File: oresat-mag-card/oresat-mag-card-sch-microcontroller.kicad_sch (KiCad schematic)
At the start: 31 parts, among them U7 MCXN947VKLT, U8 TCAN330, Y1 24 MHz

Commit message: Final mag card
Lots of polishing around best practices layout. Put in giant hole to thread the MTs from below if required for the 3U CubeSats. Cleaned up power layer, added stitching vias, updated readme.
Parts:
- C13, C14, C15, C16, C17, C18, C19, C20, C21, C22, C23, C24, C25, C26, C27, C28, C29, C30, C70, D4, R47, R76, U8, Y1: DIST DigiKey -> (none)
- FB1, L2: DIS DIgiKey -> DigiKey
- R45: DIS Digi-Key -> DigiKey
- R46, R48, U7: DIS (none) -> DigiKey; DIST DigiKey -> (none)
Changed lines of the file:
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@@
 	(title_block
 		(title "OreSat Mag Card")
-		(date "2026-04-02")
+		(date "2026-04-07")
 		(rev "v1.0")
 		(company "Portland State Aerospace Society")
@@
 			)
 		)
-		(property "DIST" "DigiKey"
+		(property "DIST" ""
 			(at 148.59 190.5 0)
 			(effects
@@
 			)
 		)
-		(property "DIST" "DigiKey"
+		(property "DIST" ""
 			(at 345.44 252.73 0)
 			(effects
@@
 			)
 		)
-		(property "DIST" "DigiKey"
+		(property "DIST" ""
 			(at 397.51 96.52 0)
 			(effects
@@
 			)
 		)
-		(property "DIST" "DigiKey"
+		(property "DIST" ""
 			(at 353.06 252.73 0)
 			(effects
@@
 			)
 		)
-		(property "DIS" "Digi-Key"
+		(property "DIS" "DigiKey"
 			(at 116.84 198.12 0)
 			(effects
@@
 			)
 		)
-		(property "DIST" "DigiKey"
+		(property "DIST" ""
 			(at 101.6 210.82 0)
 			(effects
@@
 			)
 		)
-		(property "DIST" "DigiKey"
+		(property "DPN" "568-MCXN947VDFT-ND"
 			(at 236.22 184.15 0)
 			(effects
@@
 			)
 		)
-		(property "DPN" "568-MCXN947VDFT-ND"
+		(property "DIS" "DigiKey"
+			(at 236.22 184.15 0)
+			(effects
+				(font
+					(size 1.27 1.27)
+				)
+				(hide yes)
+			)
+		)
+		(property "DIST" ""
 			(at 236.22 184.15 0)
 			(effects
@@
 			)
 		)
-		(property "DIS" "DIgiKey"
+		(property "DIS" "DigiKey"
 			(at 375.92 110.49 90)
 			(effects
@@
 			)
 		)
-		(property "DIST" "DigiKey"
+		(property "DIST" ""
 			(at 377.19 252.73 0)
 			(effects
@@
 			)
 		)
-		(property "DIST" "DigiKey"
+		(property "DIST" ""
 			(at 322.58 252.73 0)
 			(effects
@@
 			)
 		)
-		(property "DIST" "DigiKey"
+		(property "DIST" ""
 			(at 330.2 252.73 0)
 			(effects
@@
 			)
 		)
-		(property "DIST" "DigiKey"
+		(property "DIST" ""
 			(at 368.3 252.73 0)
 			(effects
@@
 			)
 		)
-		(property "DIST" "DigiKey"
+		(property "DPN" "RMCF0603FT4K70CT-ND"
 			(at 285.75 190.5 0)
 			(effects
@@
 			)
 		)
-		(property "DPN" "RMCF0603FT4K70CT-ND"
+		(property "MFR" "Stackpole Electronics"
 			(at 285.75 190.5 0)
 			(effects
@@
 			)
 		)
-		(property "MFR" "Stackpole Electronics"
+		(property "MPN" "RMCF0603FT4K70"
 			(at 285.75 190.5 0)
 			(effects
@@
 			)
 		)
-		(property "MPN" "RMCF0603FT4K70"
+		(property "DIS" "DigiKey"
+			(at 285.75 190.5 0)
+			(effects
+				(font
+					(size 1.27 1.27)
+				)
+				(hide yes)
+			)
+		)
+		(property "DIST" ""
 			(at 285.75 190.5 0)
 			(effects
@@
 			)
 		)
-		(property "DIST" "DigiKey"
+		(property "DIST" ""
 			(at 116.84 204.47 90)
 			(effects
@@
 			)
 		)
-		(property "DIST" "DigiKey"
+		(property "DIST" ""
 			(at 311.15 39.37 0)
 			(effects
@@
 			)
 		)
-		(property "DIST" "DigiKey"
+		(property "DPN" "568-MCXN947VDFT-ND"
 			(at 344.17 82.55 0)
 			(effects
@@
 			)
 		)
-		(property "DPN" "568-MCXN947VDFT-ND"
+		(property "DIS" "DigiKey"
+			(at 344.17 82.55 0)
+			(effects
+				(font
+					(size 1.27 1.27)
+				)
+				(hide yes)
+			)
+		)
+		(property "DIST" ""
 			(at 344.17 82.55 0)
 			(effects
@@
 			)
 		)
-		(property "DIST" "DigiKey"
+		(property "DIST" ""
 			(at 314.96 252.73 0)
 			(effects
@@
 			)
 		)
-		(property "DIST" "DigiKey"
+		(property "DIST" ""
 			(at 337.82 252.73 0)
 			(effects
@@
 			)
 		)
-		(property "DIST" "DigiKey"
+		(property "DPN" "568-MCXN947VDFT-ND"
 			(at 236.22 128.27 0)
 			(effects
@@
 			)
 		)
-		(property "DPN" "568-MCXN947VDFT-ND"
+		(property "DIS" "DigiKey"
+			(at 236.22 128.27 0)
+			(effects
+				(font
+					(size 1.27 1.27)
+				)
+				(hide yes)
+			)
+		)
+		(property "DIST" ""
 			(at 236.22 128.27 0)
 			(effects
@@
 			)
 		)
-		(property "DIST" "DigiKey"
+		(property "DIST" ""
 			(at 311.15 48.26 0)
 			(effects
@@
 			)
 		)
-		(property "DIST" "DigiKey"
-			(at 95.25 207.01 90)
+		(property "DIST" ""
+			(at 95.25 207.01 0)
 			(effects
 				(font
@@
 			)
 		)
-		(property "DIST" "DigiKey"
+		(property "DPN" "568-MCXN947VDFT-ND"
 			(at 236.22 86.36 0)
 			(effects
@@
 			)
 		)
-		(property "DPN" "568-MCXN947VDFT-ND"
+		(property "DIS" "DigiKey"
+			(at 236.22 86.36 0)
+			(effects
+				(font
+					(size 1.27 1.27)
+				)
+				(hide yes)
+			)
+		)
+		(property "DIST" ""
 			(at 236.22 86.36 0)
 			(effects
@@
 			)
 		)
-		(property "DIS" "DIgiKey"
+		(property "DIS" "DigiKey"
 			(at 403.86 86.36 0)
 			(effects
@@
 			)
 		)
-		(property "DIST" "DigiKey"
+		(property "DPN" "568-MCXN947VDFT-ND"
 			(at 237.49 226.06 0)
 			(effects
@@
 			)
 		)
-		(property "DPN" "568-MCXN947VDFT-ND"
+		(property "DIS" "DigiKey"
+			(at 237.49 226.06 0)
+			(effects
+				(font
+					(size 1.27 1.27)
+				)
+				(hide yes)
+			)
+		)
+		(property "DIST" ""
 			(at 237.49 226.06 0)
 			(effects
@@
 			)
 		)
-		(property "DIST" "DigiKey"
+		(property "DPN" "RMCF0603FT4K70CT-ND"
 			(at 290.83 190.5 0)
 			(effects
@@
 			)
 		)
-		(property "DPN" "RMCF0603FT4K70CT-ND"
+		(property "MFR" "Stackpole Electronics"
 			(at 290.83 190.5 0)
 			(effects
@@
 			)
 		)
-		(property "MFR" "Stackpole Electronics"
+		(property "MPN" "RMCF0603FT4K70"
 			(at 290.83 190.5 0)
 			(effects
@@
 			)
 		)
-		(property "MPN" "RMCF0603FT4K70"
+		(property "DIS" "DigiKey"
+			(at 290.83 190.5 0)
+			(effects
+				(font
+					(size 1.27 1.27)
+				)
+				(hide yes)
+			)
+		)
+		(property "DIST" ""
 			(at 290.83 190.5 0)
 			(effects
@@
 			)
 		)
-		(property "DIST" "DigiKey"
+		(property "DIST" ""
 			(at 288.29 167.64 0)
 			(effects
@@
 			)
 		)
-		(property "DIST" "DigiKey"
+		(property "DIST" ""
 			(at 374.65 128.27 0)
 			(effects
@@
 			)
 		)
-		(property "DIST" "DigiKey"
+		(property "DIST" ""
 			(at 389.89 106.68 0)
 			(effects
@@
 			)
 		)
-		(property "DIST" "DigiKey"
+		(property "DIST" ""
 			(at 88.9 210.82 0)
 			(effects
@@
 			)
 		)
-		(property "DIST" "DigiKey"
+		(property "DPN" "568-MCXN947VDFT-ND"
 			(at 69.85 181.61 0)
 			(effects
@@
 			)
 		)
-		(property "DPN" "568-MCXN947VDFT-ND"
+		(property "DIS" "DigiKey"
+			(at 69.85 181.61 0)
+			(effects
+				(font
+					(size 1.27 1.27)
+				)
+				(hide yes)
+			)
+		)
+		(property "DIST" ""
 			(at 69.85 181.61 0)
 			(effects
@@
 			)
 		)
-		(property "DIST" "DigiKey"
+		(property "DIST" ""
 			(at 379.73 114.3 0)
 			(effects
@@
 			)
 		)
-		(property "DIST" "DigiKey"
+		(property "DIST" ""
 			(at 367.03 128.27 0)
 			(effects
@@
 			)
 		)
-		(property "DIST" "DigiKey"
+		(property "DIST" ""
 			(at 163.83 171.45 0)
 			(effects
@@
 			)
 		)
-		(property "DIST" "DigiKey"
+		(property "DIST" ""
 			(at 375.92 71.12 90)
 			(effects
@@
 			)
 		)
-		(property "DIST" "DigiKey"
+		(property "DPN" "568-MCXN947VDFT-ND"
 			(at 69.85 106.68 0)
 			(effects
@@
 			)
 		)
-		(property "DPN" "568-MCXN947VDFT-ND"
+		(property "DIS" "DigiKey"
+			(at 69.85 106.68 0)
+			(effects
+				(font
+					(size 1.27 1.27)
+				)
+				(hide yes)
+			)
+		)
+		(property "DIST" ""
 			(at 69.85 106.68 0)
 			(effects
@@
 			)
 		)
-		(property "DIST" "DigiKey"
+		(property "DIST" ""
 			(at 360.68 252.73 0)
 			(effects

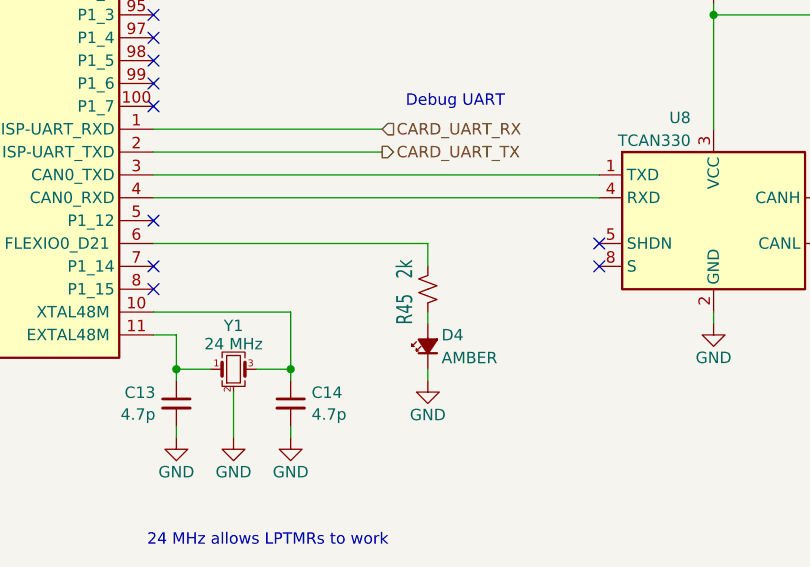
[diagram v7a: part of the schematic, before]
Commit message: Upgraded to kiCad 10, updated BOM during fabrication woes with Colorodo PCBA, no change in PCB
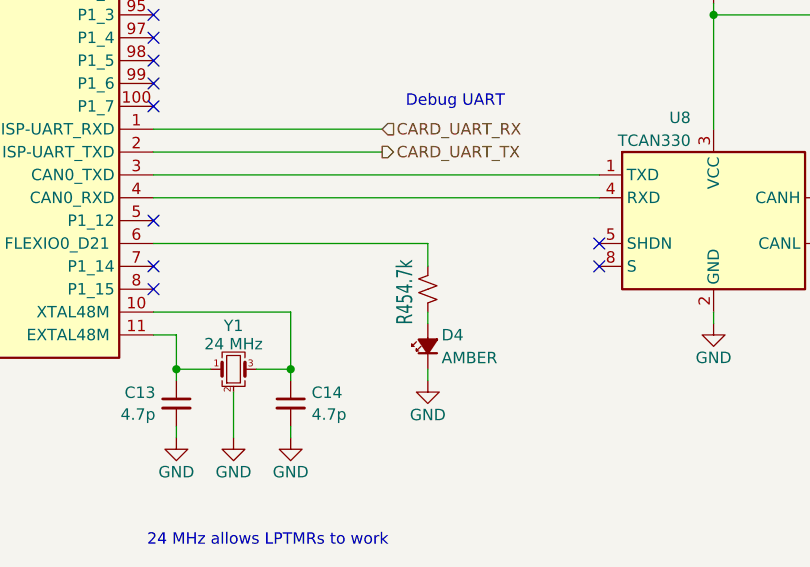
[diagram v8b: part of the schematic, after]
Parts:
- C13, C14, C15, C16, C17, C18, C19, C20, C21, C22, C23, C24, C25, C26, C27, C28, C29, C30, C70, D4, FB1, L2, R46, R47, R48, R76, U8, Y1: DIST (none) -> DigiKey
- R45: value 2k -> 4.7k; DIST (none) -> DigiKey; DPN RMCF0603FT2K00TR-ND -> RMCF0603FT4K70CT-ND; MFR Stackpole Electronics Inc -> Stackpole Electronics; MPN RMCF0603FT2K00 -> RMCF0603FT4K70
- U7: DIST (none) -> Mouser; DPN 568-MCXN947VDFT-ND -> 771-MCXN947VKLT; MPN MCXN947VDFT -> MCXN947VKLT
